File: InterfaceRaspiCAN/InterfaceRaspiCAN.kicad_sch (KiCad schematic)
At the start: 33 parts, among them J1 Raspberry_Pi_2_3, J10 Conn_02x01, J11 Conn_02x01, J12 Conn_02x01, J13 Conn_01x02, J14 Conn_01x02, J15 Conn_01x02, J16 Conn_01x02, J17 Conn_01x02, J18 Conn_01x02, J19 Conn_01x02, J2 CAN1, J20 Conn_01x02, J3 CAN2, J4 I2C1_5, J5 I2C2_5, J6 I2C3_5, J7 I2C4_5, U1 MCP2517FD-xSL, U2 MCP2558FD-xSN, U3 PCF8575, U4 PESD1CAN, Y1 40MHz

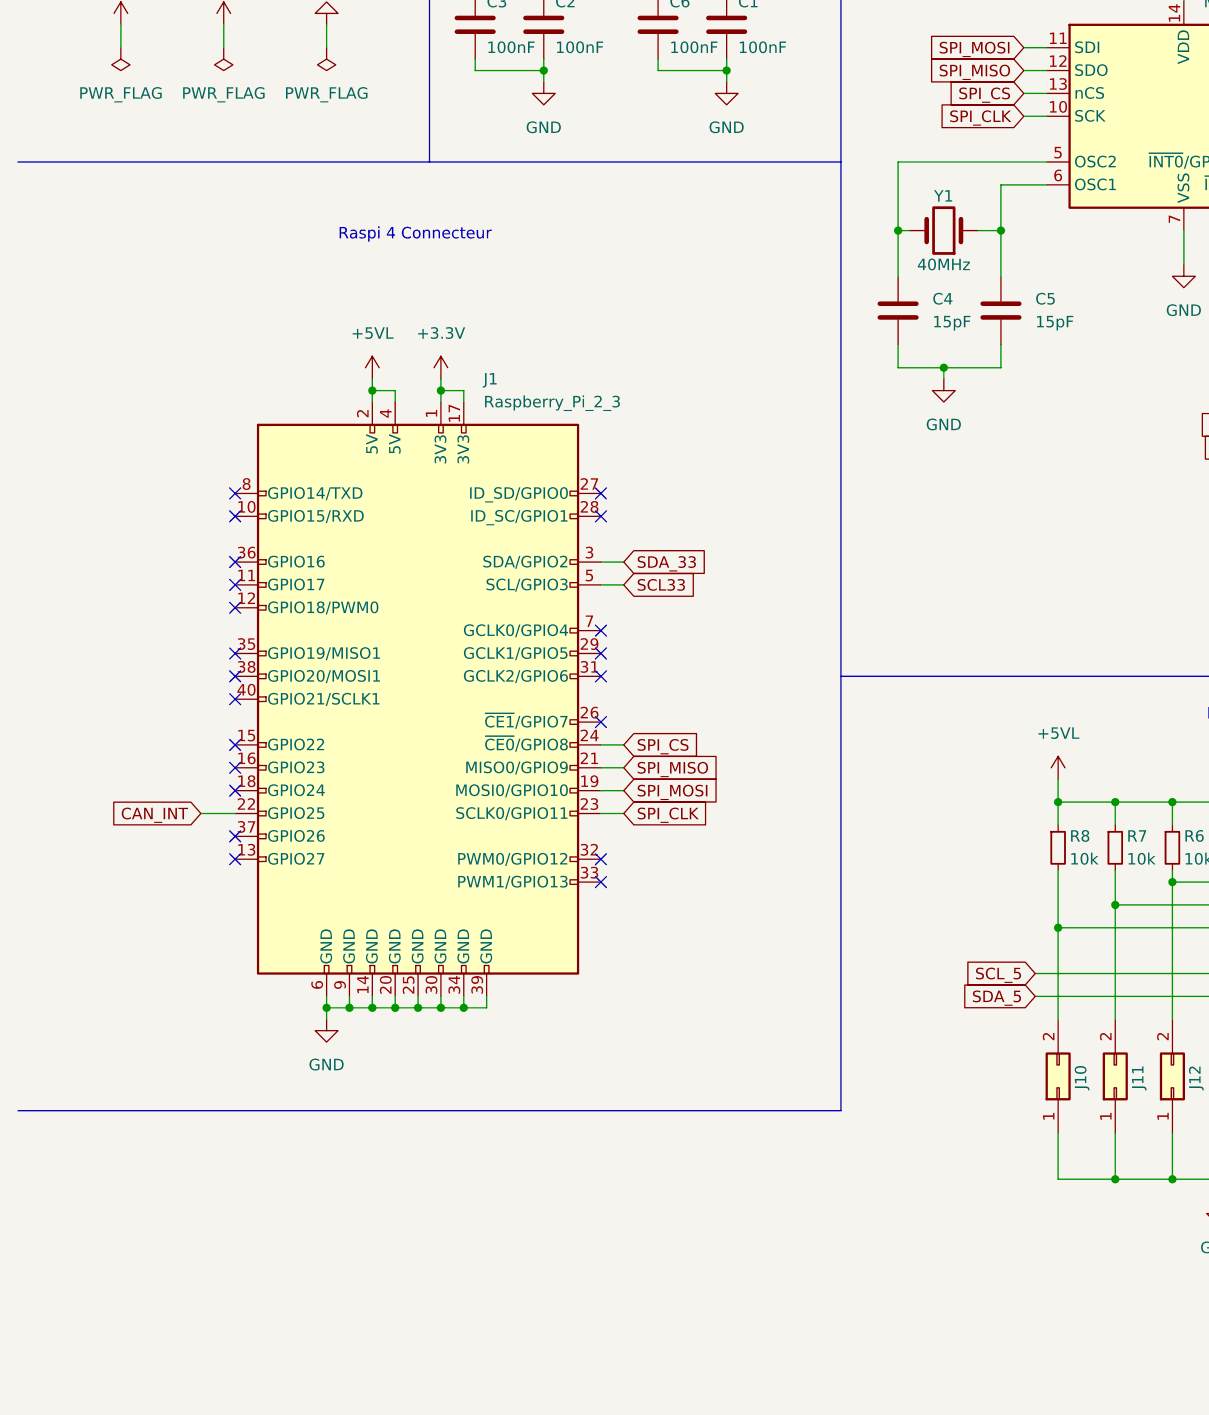
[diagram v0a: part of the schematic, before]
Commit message: Add PCB for RaspiCAN
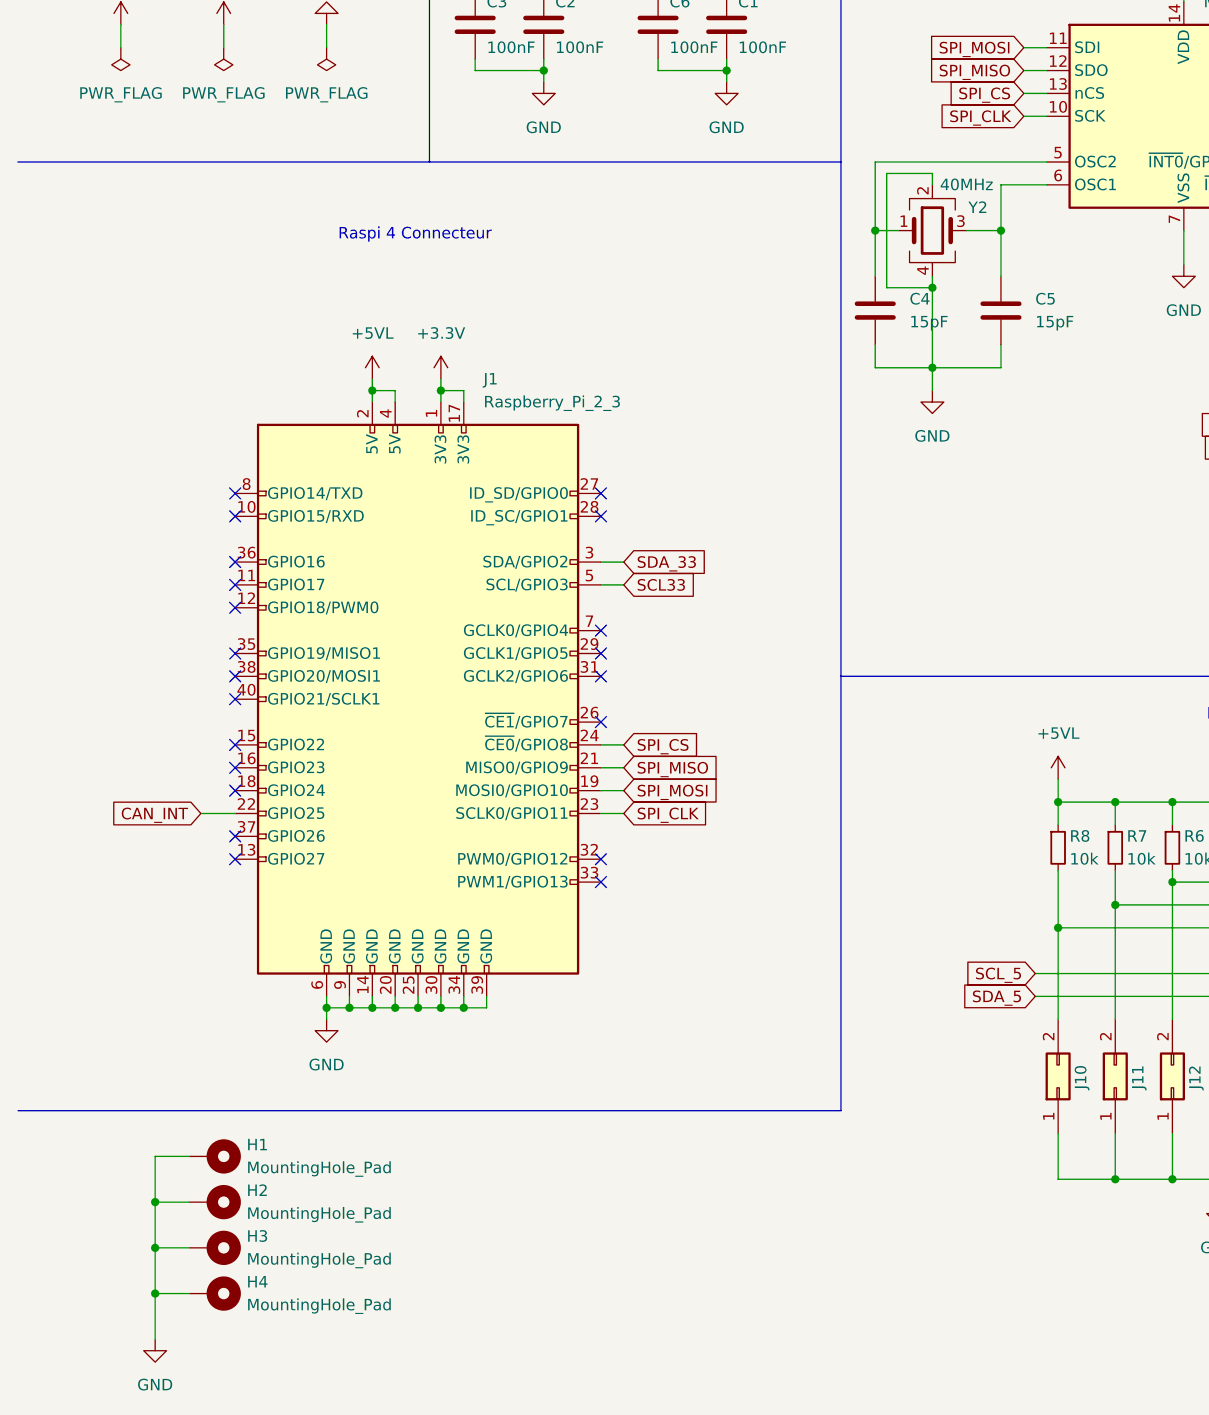
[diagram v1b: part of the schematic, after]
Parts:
- removed Y1: 40MHz, symbol Device:Crystal
- added H1, H2, H3, H4: MountingHole_Pad, MountingHole:MountingHole_2.7mm_M2.5_Pad_Via, symbol Mechanical:MountingHole_Pad
- added Y2: 40MHz, Crystal:Crystal_SMD_3225-4Pin_3.2x2.5mm_HandSoldering, symbol Device:Crystal_GND24
- C1, C2, C3, C4, C5, C6: footprint (none) -> Capacitor_SMD:C_0402_1005Metric_Pad0.74x0.62mm_HandSolder
- J10, J11, J12: footprint (none) -> Jumper:SolderJumper-2_P1.3mm_Bridged_RoundedPad1.0x1.5mm
- J13, J14, J15, J16, J17, J18, J19, J20: footprint (none) -> Connector_JST:JST_EH_B2B-EH-A_1x02_P2.50mm_Vertical
- J2, J3, J4, J5, J6, J7: footprint (none) -> Connector_JST:JST_EH_B4B-EH-A_1x04_P2.50mm_Vertical
- R1, R6, R7, R8: footprint (none) -> Resistor_SMD:R_0805_2012Metric_Pad1.20x1.40mm_HandSolder
- U3: footprint IPC7351-Nominal:SOP65P775X200-24 -> Package_SO:SSOP-24_5.3x8.2mm_P0.65mm
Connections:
- net GND: now also H1.1, H2.1, H3.1, H4.1, Y2.2, Y2.4
- net at C5.1, U1.6 (OSC1): now also Y2.3
- net at C4.1, U1.5 (OSC2): now also Y2.1
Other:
- moved on the sheet: C4

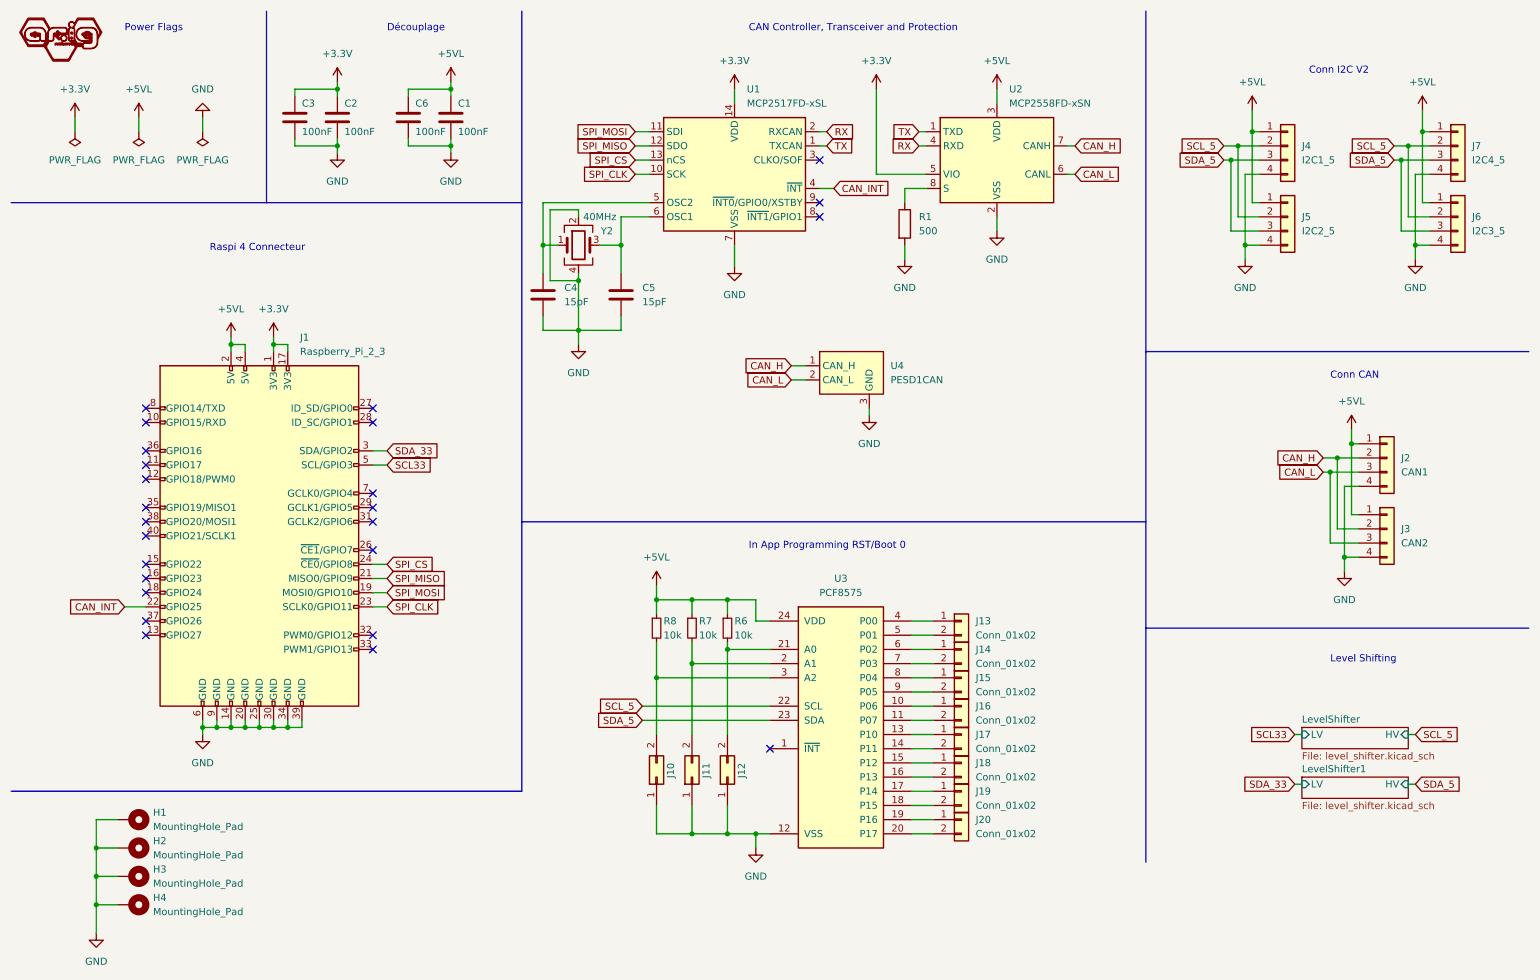
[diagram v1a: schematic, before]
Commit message: Changes from discussion on meetings
- Remove 2x I2C connectors
- Remove 4x InApp programming connectors
- Change PCF8575 to PCF8574
- Change a half connectors to horizontal version
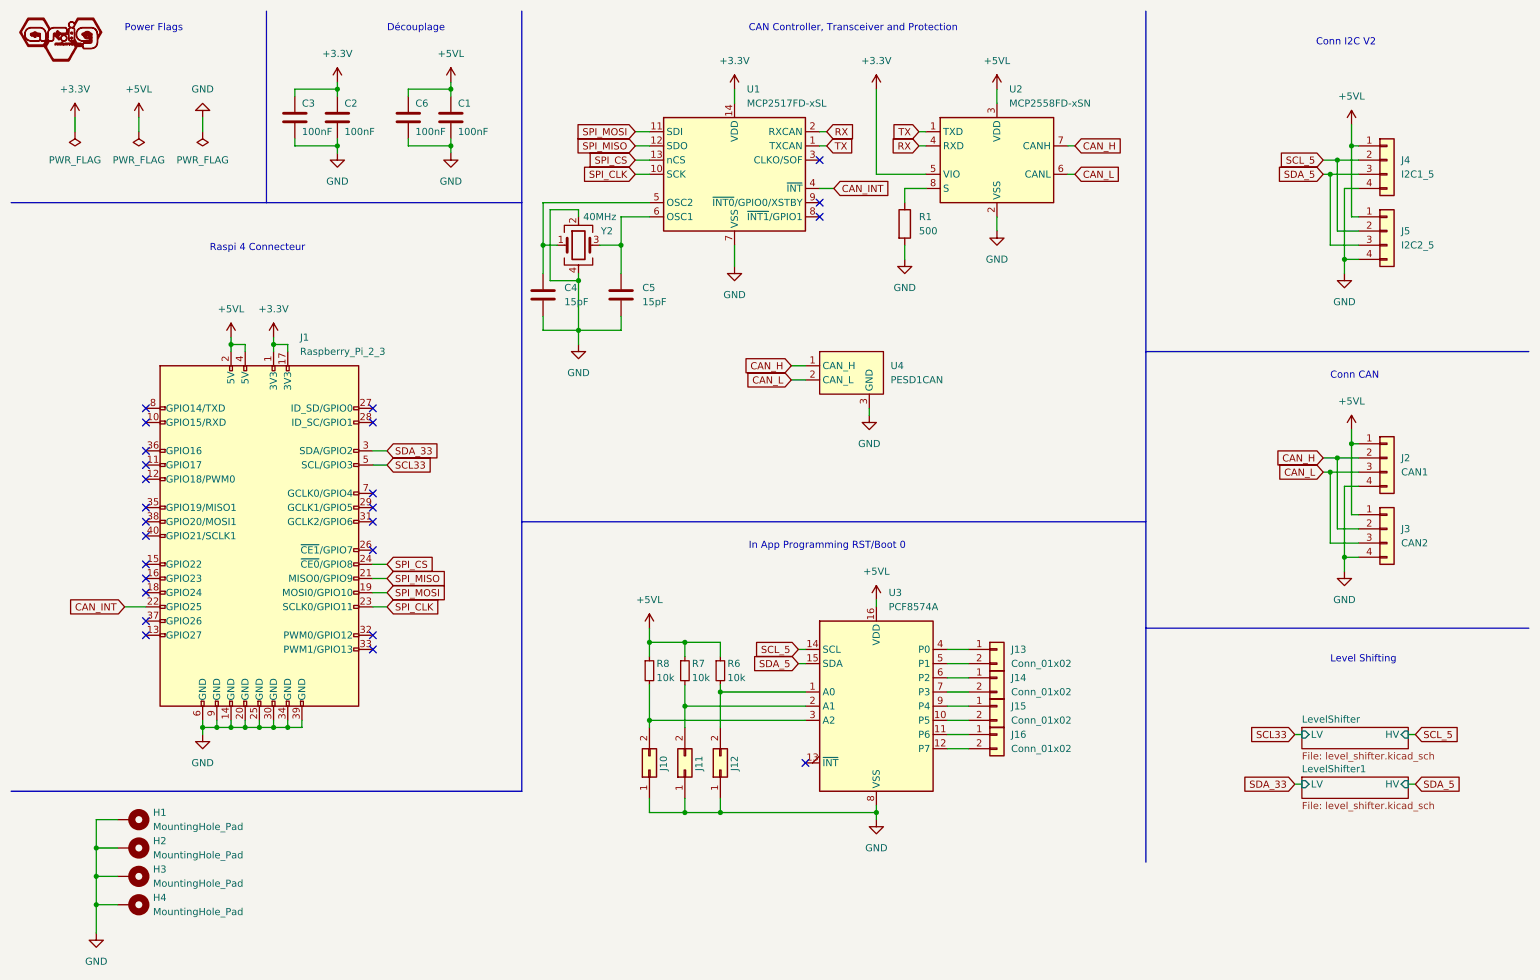
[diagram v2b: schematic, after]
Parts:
- removed J17, J18, J19, J20: Conn_01x02, Connector_JST:JST_EH_B2B-EH-A_1x02_P2.50mm_Vertical, symbol Connector_Generic:Conn_01x02
- removed J6: I2C3_5, Connector_JST:JST_EH_B4B-EH-A_1x04_P2.50mm_Vertical, symbol Connector_Generic:Conn_01x04
- removed J7: I2C4_5, Connector_JST:JST_EH_B4B-EH-A_1x04_P2.50mm_Vertical, symbol Connector_Generic:Conn_01x04
- removed U3: PCF8575, Package_SO:SSOP-24_5.3x8.2mm_P0.65mm, symbol ARIG:PCF8575
- added U3: PCF8574A, Package_SO:SOIC-16W_7.5x10.3mm_P1.27mm, symbol Interface_Expansion:PCF8574A
- J10, J11, J12: footprint Jumper:SolderJumper-2_P1.3mm_Bridged_RoundedPad1.0x1.5mm -> Jumper:SolderJumper-2_P1.3mm_Open_RoundedPad1.0x1.5mm
- J15, J16: footprint Connector_JST:JST_EH_B2B-EH-A_1x02_P2.50mm_Vertical -> Connector_JST:JST_EH_S2B-EH_1x02_P2.50mm_Horizontal
- J3, J5: footprint Connector_JST:JST_EH_B4B-EH-A_1x04_P2.50mm_Vertical -> Connector_JST:JST_EH_S4B-EH_1x04_P2.50mm_Horizontal
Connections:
- net +5VL: now also U3.16 (VDD)
- net GND: now also U3.8 (VSS)
- net SCL_5: now also U3.14 (SCL)
- net SDA_5: now also U3.15 (SDA)
- net at J11.2 (Pin_2), R7.2: now also U3.2 (A1)
- net at J12.2 (Pin_2), R6.2: now also U3.1 (A0)
- net at J16.1 (Pin_1): now also U3.11 (P6)
- net at J16.2 (Pin_2): now also U3.12 (P7)
- net at J10.2 (Pin_2), R8.2: now also U3.3 (A2)
- net at J13.1 (Pin_1): now also U3.4 (P0)
- net at J13.2 (Pin_2): now also U3.5 (P1)
- net at J14.1 (Pin_1): now also U3.6 (P2)
- net at J14.2 (Pin_2): now also U3.7 (P3)
- net at J15.1 (Pin_1): now also U3.9 (P4)
- net at J15.2 (Pin_2): now also U3.10 (P5)
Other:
- moved on the sheet: J10, J11, J12, J13, J14, J15, J16, J4, J5, R6, R7, R8
